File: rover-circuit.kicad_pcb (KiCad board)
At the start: 4 copper layers, 78 x 75.3 mm, 64 parts, among them J1 Battery Connector, J2 USB_C_Receptacle_USB2.0_14P, J3 Conn_01x04, J5 Raspberry_Pi_2_3, J6 Conn_02x07_Odd_Even, M1 Motor_DC, M2 Motor_DC, SW1 SW_EN, SW2 SW_IO0, U1 ESP32-C6-MINI-1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

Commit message: more on routing and schematic
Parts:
- added C10: 100uF, Capacitor_SMD:CP_Elec_6.3x5.4, F.Cu at (149.3, 74.8)
- added C11: 10uF, Capacitor_SMD:C_0805_2012Metric, F.Cu at (153.9, 79.5)
- added C8: 2.2uF, Capacitor_SMD:C_0603_1608Metric, F.Cu at (144.3, 77.8)
- added C9: 10nF, Capacitor_SMD:C_0603_1608Metric, F.Cu at (139.2, 79.0)
- added R10: 200m, Resistor_SMD:R_1206_3216Metric, F.Cu at (144.3, 74.0)
- added R9: 200m, Resistor_SMD:R_1206_3216Metric, F.Cu at (136.4, 74.0)
- added U10: LTC2954CDDB-1-PBF, Package_DFN_QFN:DFN-8-1EP_2x3mm_P0.5mm_EP0.61x2.2mm, F.Cu at (137.7, 90.9)
- moved C26 188.1 mm to (139.9, 91.7), turned to -90 degrees
- moved C21 25.1 mm to (129.4, 98.3), turned to 0 degrees
- moved C22 25.1 mm to (133.1, 91.6), turned to 180 degrees
- moved L3 23.6 mm to (128.2, 94.4), turned to 180 degrees
- moved C20 21.7 mm to (129.4, 100.3), turned to 0 degrees
- moved U7 19.4 mm to (133.7, 94.4), turned to 180 degrees
- moved C18 15.5 mm to (141.7, 97.2), turned to 90 degrees
- moved C19 15.0 mm to (132.7, 96.9)
- moved C28 12.5 mm to (144.4, 93.8), turned to 180 degrees
- moved C17 11.7 mm to (144.4, 95.8), turned to 180 degrees
- moved U9 11.5 mm to (144.5, 98.4), turned to 0 degrees
- moved D2 10.8 mm to (124.9, 68.6), turned to 150 degrees
- moved D1 10.7 mm to (124.0, 70.2), turned to 150 degrees
- moved R8 9.21 mm to (127.6, 70.1), turned to -30 degrees
- moved R1 9.14 mm to (126.7, 71.7), turned to -30 degrees
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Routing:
- net /Battery Recharger/CBSET_PIN: track 34.5 -> 0.00 mm, vias 2 -> 0
- net /Power Rails/EN: track 0.00 -> 24.2 mm, vias 0 -> 4
- net /Battery Recharger/TS: track 26.5 -> 4.53 mm, vias 1 -> 0
- net /Battery Recharger/REGN: track 19.8 -> 6.03 mm, vias 2 -> 0
- net Net-(U2-~{PG}): track 12.9 -> 0.00 mm
- net Net-(U2-STAT): track 12.1 -> 0.00 mm
- net +5V: track 0.00 -> 9.24 mm, vias 1 -> 2
- net Net-(M2--): track 0.00 -> 8.65 mm
- net Net-(M2-+): track 0.00 -> 8.51 mm
- net Net-(M1-+): track 0.00 -> 8.48 mm
- net Net-(M1--): track 0.00 -> 8.35 mm
- net Net-(U3-BISEN): track 0.00 -> 7.67 mm, vias 0 -> 4
- net Net-(U3-AISEN): track 0.00 -> 7.60 mm, vias 0 -> 5
- net Net-(U7-SW): track 0.00 -> 5.64 mm
- net Net-(U9-SW): track 0.00 -> 2.49 mm
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- removed copper zone on F.Cu, net +3V3
- removed copper zone on B.Cu, net +BATT
- removed copper zone on F.Cu, net Net-(U7-SW)
- removed copper zone on B.Cu, net VBUS

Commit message: some improvements
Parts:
- moved C11 10.6 mm to (143.5, 81.2), turned to -90 degrees
- moved J1 0.69 mm to (135.6, 62.2)
- moved U1 0.51 mm to (173.8, 63.4)
- moved C1 0.51 mm to (165.6, 61.0)
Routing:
- net /Battery Recharger/CBSET_PIN: track 0.00 -> 32.2 mm, vias 0 -> 1
- net /Battery Recharger/REGN: track 6.03 -> 22.1 mm, vias 0 -> 2
- net /Battery Recharger/TS: track 4.53 -> 20.5 mm, vias 0 -> 1
- net Net-(U2-~{PG}): track 0.00 -> 11.7 mm
- net +6V: track 1.84 -> 13.5 mm, vias 0 -> 2
- net Net-(U2-STAT): track 0.00 -> 11.2 mm
- net /Power Rails/EN: track 24.2 -> 29.1 mm, vias 4 -> 3
- net /Battery Recharger/SCL: track 0.00 -> 4.64 mm, vias 0 -> 1
- net Net-(U3-VINT): track 0.00 -> 4.37 mm
- net /Battery Recharger/SDA: track 0.00 -> 3.79 mm, vias 0 -> 1
- net /Battery Recharger/CD: track 0.00 -> 2.92 mm, vias 0 -> 1
- net Net-(U5-BST): track 0.00 -> 1.80 mm
- net VBUS: vias 0 -> 4
- net GND: vias 10 -> 11
- net +BATT: vias 0 -> 19
- added copper zone on B.Cu, net +BATT
- added copper zone on B.Cu, net VBUS

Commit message: updates
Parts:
- added SW3: SW_Push, Button_Switch_SMD:SW_SPST_B3U-1000P, F.Cu at (225.5, 122.2)
- moved SW1 172.4 mm to (163.1, 66.8), turned to 90 degrees
- moved J6 161.5 mm to (149.1, 115.4)
- moved SW2 150.8 mm to (185.3, 71.9), turned to 180 degrees
- moved D3 65.3 mm to (151.5, 93.8)
- moved R15 65.3 mm to (148.4, 93.8)
- moved J1 2.06 mm to (137.6, 62.2)
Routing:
- net /Rasbpberry PI/SDA: track 0.00 -> 25.2 mm
- net +5V: track 9.24 -> 30.6 mm
- net /Rasbpberry PI/SCL: track 0.00 -> 19.5 mm
- net /Battery Recharger/CBSET_IN: track 0.00 -> 8.79 mm
- net /Battery Recharger/CBSET_PIN: track 32.2 -> 28.2 mm
- net Net-(U5-SW): track 1.80 -> 0.00 mm
- net /Battery Recharger/REGN: track 22.1 -> 21.3 mm
- net /Battery Recharger/TS: track 20.5 -> 20.3 mm, vias 1 -> 2
- net VBUS: vias 4 -> 8
- net GND: vias 11 -> 16
- removed copper zone on F.Cu, net /Battery Recharger/CBSET_IN

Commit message: progress on routing
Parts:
- added C27: 0.1uF, Resistor_SMD:R_0805_2012Metric, F.Cu at (165.5, 66.3)
- added C29: 100nF, Capacitor_SMD:C_0603_1608Metric, F.Cu at (215.8, 85.2)
- added C30: 100nF, Capacitor_SMD:C_0603_1608Metric, F.Cu at (215.8, 87.7)
- added R16: 4.7k, Resistor_SMD:R_0603_1608Metric, F.Cu at (153.3, 63.7)
- added R17: 4.7k, Resistor_SMD:R_0603_1608Metric, F.Cu at (155.9, 63.7)
- added R18: 10k, Resistor_SMD:R_0603_1608Metric, F.Cu at (221.8, 85.2)
- added R19: 470, Resistor_SMD:R_0603_1608Metric, F.Cu at (221.8, 87.7)
- added R20: 470, Resistor_SMD:R_0603_1608Metric, F.Cu at (221.8, 90.2)
- added U11: BMI270, Package_LGA:Bosch_LGA-14_3x2.5mm_P0.5mm, F.Cu at (237.2, 74.5)
- U1: value ESP32-C6-MINI-1 -> MMC5983MA; footprint RF_Module:ESP32-C6-MINI-1 -> Package_LGA:LGA-16_3x3mm_P0.5mm
- U6: value MPU-6050 -> ESP32-C6-WROOM-1-N8; footprint Sensor_Motion:InvenSense_QFN-24_4x4mm_P0.5mm -> lib_fp:XCVR_ESP32-C6-WROOM-1-N8
- moved U6 194.5 mm to (182.2, 86.0), turned to -90 degrees
- moved SW3 106.2 mm to (124.7, 88.7), turned to 0 degrees
- moved U1 66.9 mm to (236.9, 85.5)
- moved SW1 45.8 mm to (208.7, 71.5)
- moved DWM1 28.0 mm to (174.4, 59.6), turned to 0 degrees
- moved SW2 19.9 mm to (205.2, 71.5), turned to 90 degrees
- moved J6 4.01 mm to (145.3, 114.2)
- moved C1 3.13 mm to (163.3, 59.0), turned to 90 degrees
- moved R3 0.58 mm to (129.1, 76.4)
- moved C6 0.51 mm to (125.4, 84.4)
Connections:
- net /Battery Recharger/~{INT} renamed Net-(U2-~{INT})
- net /Motor Driver/AIN1 renamed /MCU/AIN1
- net /Motor Driver/AIN2 renamed /MCU/AIN2
- net /Motor Driver/BIN1 renamed /MCU/BIN1
- net /Motor Driver/BIN2 renamed /MCU/BIN2
- net /UWB/UWB_RST renamed /MCU/UWB_RST
- net /UWB/UWB_WAKEUP renamed /MCU/UWB_WUP
- net /UWB/UWB_~{CS} renamed /MCU/UWB_~{CS}
- DWM1 pad 22: /UWB/UWB_IRQ -> /MCU/UWB_IRQ
- R3 pad 1: +3V3 -> /Battery Recharger/REGN
- SW2 pad 2: /MCU/IO0 -> /MCU/IO9
- U1 pad 1: GND -> /Battery Recharger/SCL
- U1 pad 10: unconnected-(U1-IO5-Pad10) -> Net-(U1-CAP)
- U1 pad 13: unconnected-(U1-IO1-Pad13) -> +3V3
- U1 pad 14: GND -> unconnected-(U1-NC-Pad14)
- U1 pad 15: /Battery Recharger/SDA -> unconnected-(U1-INT-Pad15)
- U1 pad 16: /Battery Recharger/SCL -> /Battery Recharger/SDA
- U1 pad 2: GND -> +3V3
- U1 pad 3: +3V3 -> unconnected-(U1-NC-Pad3)
- U1 pad 4: unconnected-(U1-NC-Pad4) -> +3V3
- U1 pad 8: /MCU/EN -> unconnected-(U1-NC-Pad8)
- U1 pad 9: unconnected-(U1-IO4-Pad9) -> GND
- U2 pad 24: /Battery Recharger/PSEL -> unconnected-(U2-PSEL-Pad24)
- U2 pad 3: /Battery Recharger/CD -> unconnected-(U2-CD-Pad3)
- U6 pad 10: Net-(U6-REGOUT) -> unconnected-(U6-IO8-Pad10)
- U6 pad 11: GND -> unconnected-(U6-IO10-Pad11)
- U6 pad 13: +3V3 -> /MCU/USB1.D-
- U6 pad 14: unconnected-(U6-NC-Pad14) -> /MCU/USB1.D+
- U6 pad 15: unconnected-(U6-NC-Pad15) -> /MCU/IO9
- U6 pad 18: GND -> unconnected-(U6-IO20-Pad18)
- U6 pad 2: unconnected-(U6-NC-Pad2) -> +3V3
- U6 pad 20: Net-(U6-CPOUT) -> unconnected-(U6-IO22-Pad20)
- U6 pad 23: /Battery Recharger/SCL -> unconnected-(U6-IO15-Pad23)
- U6 pad 24: /Battery Recharger/SDA -> /MCU/RX0
- U6 pad 3: unconnected-(U6-NC-Pad3) -> /MCU/EN
- U6 pad 8: Net-(U6-VLOGIC) -> unconnected-(U6-IO0-Pad8)
- U6 pad 9: GND -> unconnected-(U6-IO1-Pad9)
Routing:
- net /Battery Recharger/SCL: track 4.64 -> 47.3 mm, vias 1 -> 2
- net /Battery Recharger/SDA: track 3.79 -> 42.7 mm, vias 1 -> 2
- net /Rasbpberry PI/SDA: track 25.2 -> 0.00 mm
- net /Rasbpberry PI/SCL: track 19.5 -> 0.00 mm
- net +5V: track 30.6 -> 19.7 mm
- net Net-(D3-K): track 0.00 -> 10.4 mm, vias 0 -> 2
- net /MCU/USB1.D+: track 0.00 -> 8.80 mm, vias 0 -> 1
- net /MCU/USB1.D-: track 0.00 -> 8.53 mm, vias 0 -> 1
- net /MCU/BIN1: track 0.00 -> 7.32 mm, vias 0 -> 1
- net /MCU/BIN2: track 0.00 -> 6.45 mm, vias 0 -> 1
- net /Battery Recharger/REGN: track 21.3 -> 27.6 mm, vias 2 -> 3
- net +3V3: track 0.50 -> 6.34 mm, vias 0 -> 2
- net /Battery Recharger/CD: track 2.92 -> 0.00 mm, vias 1 -> 0
- net /MCU/AIN2: track 0.00 -> 2.74 mm, vias 0 -> 1
- net /MCU/AIN1: track 0.00 -> 2.07 mm, vias 0 -> 1
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- added copper zone on F.Cu, net +3V3

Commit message: progress on routing
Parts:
- added C14: 10uF, Capacitor_SMD:C_0603_1608Metric, F.Cu at (167.2, 90.8)
- added C15: 10uF, Capacitor_SMD:C_0603_1608Metric, F.Cu at (167.1, 86.9)
- added D5: BLUE, LED_SMD:LED_0603_1608Metric, F.Cu at (164.7, 75.0)
- added D6: BLUE, LED_SMD:LED_0603_1608Metric, F.Cu at (164.7, 73.3)
- C1: footprint Capacitor_SMD:C_0402_1005Metric -> Capacitor_SMD:C_0805_2012Metric
- moved U11 78.3 mm to (159.5, 83.8)
- moved U1 72.4 mm to (164.6, 89.7)
- moved C30 59.3 mm to (156.6, 83.8), turned to -90 degrees
- moved SW1 56.8 mm to (157.3, 95.8)
- moved C29 55.1 mm to (160.8, 81.3)
- moved R20 50.8 mm to (173.7, 74.1), turned to -90 degrees
- moved SW2 49.6 mm to (162.0, 95.8)
- moved R19 48.6 mm to (175.2, 74.1), turned to -90 degrees
- moved R18 44.3 mm to (184.3, 61.6)
- moved SW3 37.4 mm to (157.2, 70.1), turned to 180 degrees
- moved C1 28.5 mm to (187.2, 74.6), turned to 0 degrees
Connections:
- U6 pad 10: unconnected-(U6-IO8-Pad10) -> /MCU/AIN2
- U6 pad 11: unconnected-(U6-IO10-Pad11) -> /MCU/AIN1
- U6 pad 12: unconnected-(U6-IO11-Pad12) -> /Motor Driver/SLEEP
- U6 pad 23: unconnected-(U6-IO15-Pad23) -> /MCU/UWB_RST
- U6 pad 26: unconnected-(U6-IO3-Pad26) -> /MCU/UWB_WUP
- U6 pad 27: unconnected-(U6-IO2-Pad27) -> /MCU/UWB_IRQ
- U6 pad 4: unconnected-(U6-IO4-Pad4) -> /MCU/CLK
- U6 pad 5: unconnected-(U6-IO5-Pad5) -> /MCU/MISO
- U6 pad 6: unconnected-(U6-IO6-Pad6) -> /MCU/MOSI
- U6 pad 7: unconnected-(U6-IO7-Pad7) -> /MCU/UWB_~{CS}
- U6 pad 8: unconnected-(U6-IO0-Pad8) -> /MCU/BIN1
- U6 pad 9: unconnected-(U6-IO1-Pad9) -> /MCU/BIN2
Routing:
- net +3V3: track 6.34 -> 140.1 mm
- net /MCU/USB1.D-: track 8.53 -> 65.8 mm, vias 1 -> 2
- net /MCU/USB1.D+: track 8.80 -> 65.0 mm, vias 1 -> 2
- net /MCU/RX0: track 0.00 -> 53.7 mm
- net /MCU/TX0: track 0.00 -> 51.4 mm
- net /MCU/UWB_WUP: track 0.00 -> 48.0 mm, vias 0 -> 2
- net /MCU/UWB_RST: track 0.00 -> 47.0 mm, vias 0 -> 2
- net /Battery Recharger/SCL: track 47.3 -> 86.9 mm
- net /Battery Recharger/SDA: track 42.7 -> 80.9 mm
- net /Motor Driver/SLEEP: track 2.07 -> 40.2 mm, vias 1 -> 2
- net /MCU/BIN1: track 7.32 -> 44.9 mm, vias 1 -> 2
- net /MCU/UWB_IRQ: track 0.00 -> 37.4 mm, vias 0 -> 2
- net /MCU/BIN2: track 6.45 -> 42.6 mm, vias 1 -> 2
- net /MCU/AIN2: track 2.74 -> 37.7 mm, vias 1 -> 2
- net /MCU/AIN1: track 2.07 -> 35.7 mm, vias 1 -> 2
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
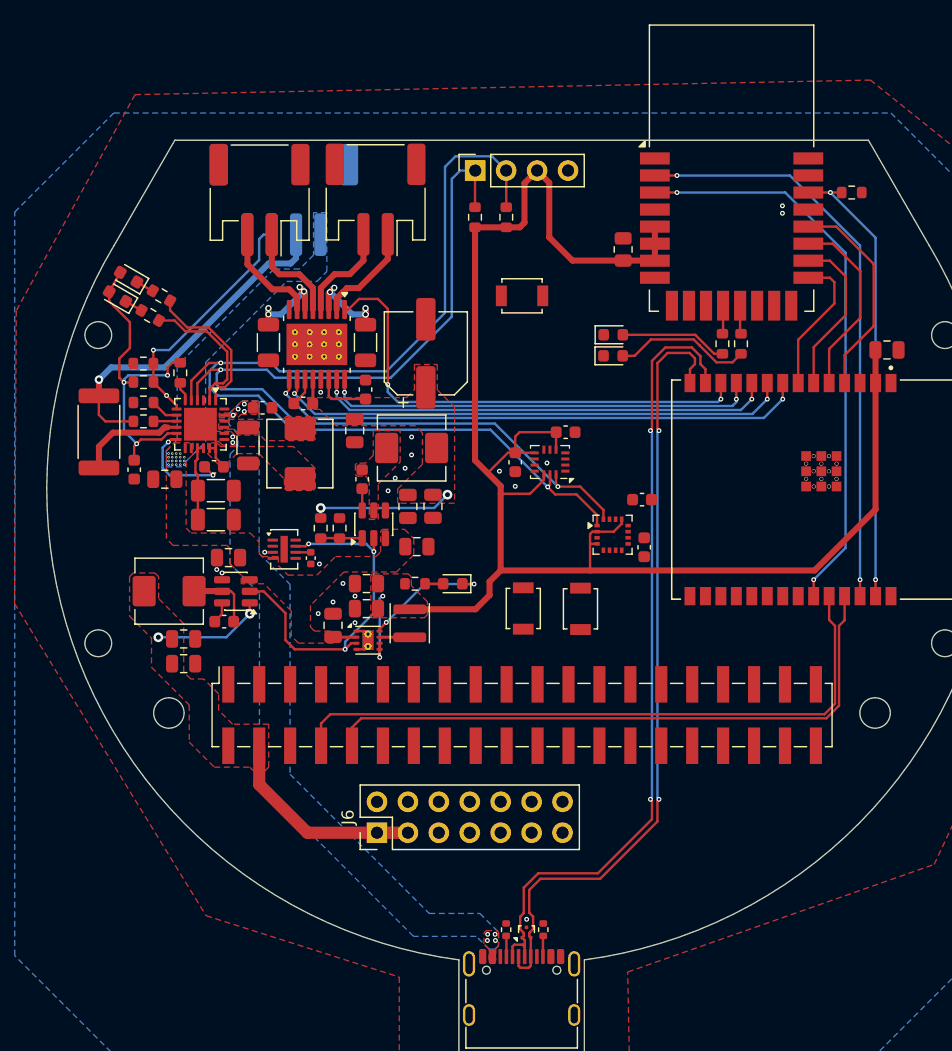
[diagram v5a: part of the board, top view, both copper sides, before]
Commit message: consolidated routing
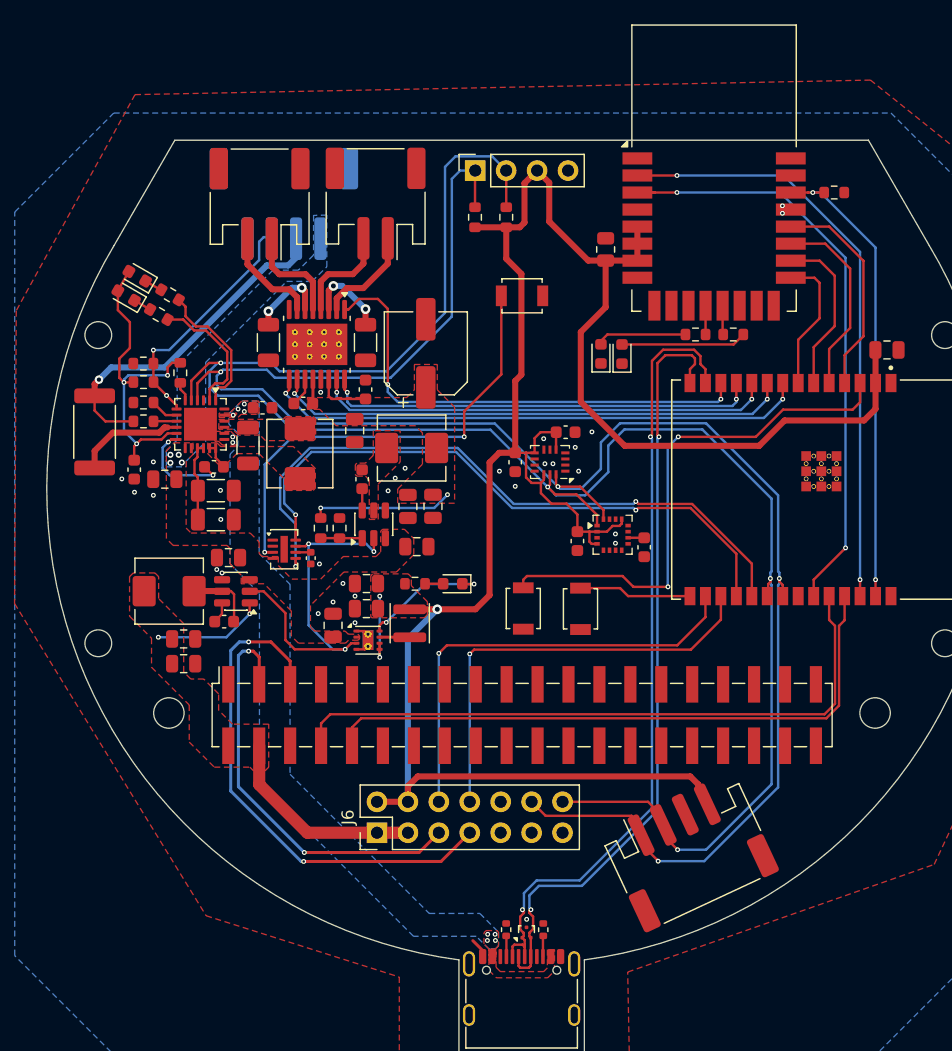
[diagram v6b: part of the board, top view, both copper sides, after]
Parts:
- added J4: Conn_01x04_Socket, Connector_JST:JST_PH_S4B-PH-SM4-TB_1x04-1MP_P2.00mm_Horizontal, F.Cu at (170.9, 115.7)
- moved C15 6.31 mm to (161.7, 90.3), turned to -90 degrees
- moved R20 2.34 mm to (171.5, 73.3), turned to 180 degrees
- moved D6 1.87 mm to (163.7, 74.9), turned to 90 degrees
- moved C27 1.44 mm to (164.1, 66.3)
- moved DWM1 1.44 mm to (173.0, 59.6)
- moved R18 1.44 mm to (182.8, 61.6)
- moved R19 0.99 mm to (174.5, 73.3), turned to 0 degrees
- moved D5 0.74 mm to (165.4, 74.9), turned to 90 degrees
- moved D1 0.71 mm to (124.7, 70.1)
- moved D2 0.71 mm to (125.6, 68.5)
- moved R1 0.71 mm to (127.4, 71.7)
- moved R8 0.71 mm to (128.3, 70.0)
- moved R5 0.36 mm to (122.1, 81.3)
- moved J1 0.33 mm to (137.6, 62.6)
- moved M1 0.33 mm to (145.2, 62.5)
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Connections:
- J5 pad 11: /Rasbpberry PI/DC -> unconnected-(J5-GPIO17-Pad11)
- J5 pad 12: /Rasbpberry PI/PWMA_1 -> unconnected-(J5-GPIO18/PWM0-Pad12)
- J5 pad 13: /Rasbpberry PI/RES -> unconnected-(J5-GPIO27-Pad13)
- J5 pad 15: /Rasbpberry PI/UWB_~{RST} -> unconnected-(J5-GPIO22-Pad15)
- J5 pad 16: /Rasbpberry PI/AIN2_1 -> unconnected-(J5-GPIO23-Pad16)
- J5 pad 18: /Rasbpberry PI/UWB_WU -> unconnected-(J5-GPIO24-Pad18)
- J5 pad 19: /Rasbpberry PI/MOSI -> unconnected-(J5-MOSI0/GPIO10-Pad19)
- J5 pad 21: /Rasbpberry PI/MISO -> unconnected-(J5-MISO0/GPIO9-Pad21)
- J5 pad 22: /Rasbpberry PI/AIN1_1 -> unconnected-(J5-GPIO25-Pad22)
- J5 pad 23: /Rasbpberry PI/CLK -> unconnected-(J5-SCLK0/GPIO11-Pad23)
- J5 pad 24: /Rasbpberry PI/UWB_~{CS} -> unconnected-(J5-~{CE0}/GPIO8-Pad24)
- J5 pad 26: /Rasbpberry PI/UWB_IRQ -> unconnected-(J5-~{CE1}/GPIO7-Pad26)
- J5 pad 27: /Rasbpberry PI/STBYB -> unconnected-(J5-ID_SD/GPIO0-Pad27)
- J5 pad 28: /Rasbpberry PI/BIN1_1 -> unconnected-(J5-ID_SC/GPIO1-Pad28)
- J5 pad 29: /Rasbpberry PI/BIN2_1 -> unconnected-(J5-GCLK1/GPIO5-Pad29)
- J5 pad 3: /Rasbpberry PI/SDA -> Net-(J5-SDA/GPIO2)
- J5 pad 31: /Rasbpberry PI/AIN2_2 -> unconnected-(J5-GCLK2/GPIO6-Pad31)
- J5 pad 32: /Rasbpberry PI/PWMB_1 -> unconnected-(J5-PWM0/GPIO12-Pad32)
- J5 pad 33: /Rasbpberry PI/PWMA_2 -> unconnected-(J5-PWM1/GPIO13-Pad33)
- J5 pad 35: /Rasbpberry PI/PWMB_2 -> unconnected-(J5-GPIO19/MISO1-Pad35)
- J5 pad 36: /Rasbpberry PI/AIN1_2 -> unconnected-(J5-GPIO16-Pad36)
- J5 pad 37: /Rasbpberry PI/BIN2_2 -> unconnected-(J5-GPIO26-Pad37)
- J5 pad 38: /Rasbpberry PI/STBYA -> unconnected-(J5-GPIO20/MOSI1-Pad38)
- J5 pad 40: /Rasbpberry PI/BIN1_2 -> unconnected-(J5-GPIO21/SCLK1-Pad40)
- J5 pad 5: /Rasbpberry PI/SCL -> Net-(J5-SCL/GPIO3)
- J5 pad 7: /Rasbpberry PI/CS -> unconnected-(J5-GCLK0/GPIO4-Pad7)
- J6 pad 10: /Rasbpberry PI/CLK -> unconnected-(J6-Pin_10-Pad10)
- J6 pad 12: /Rasbpberry PI/MISO -> /Battery Recharger/SDA
- J6 pad 14: /Rasbpberry PI/MOSI -> /Battery Recharger/SCL
- J6 pad 2: /Rasbpberry PI/SCL -> +3V3
- J6 pad 4: /Rasbpberry PI/SDA -> +3V3
- J6 pad 5: +3V3 -> Net-(J5-SDA/GPIO2)
- J6 pad 6: /Rasbpberry PI/GPIO_18 -> /MCU/IO18
- J6 pad 7: +3V3 -> Net-(J5-SCL/GPIO3)
- J6 pad 8: /Rasbpberry PI/GPIO_8 -> /MCU/IO19
- U10 pad 5: /Power Rails/~{KILL} -> /MCU/~{KILL}
- U10 pad 8: /Power Rails/~{INT} -> /MCU/~{INT}
- U6 pad 16: unconnected-(U6-IO18-Pad16) -> /MCU/IO18
- U6 pad 17: unconnected-(U6-IO19-Pad17) -> /MCU/IO19
- U6 pad 18: unconnected-(U6-IO20-Pad18) -> /MCU/~{INT}
- U6 pad 19: unconnected-(U6-IO21-Pad19) -> /MCU/~{KILL}
- U6 pad 20: unconnected-(U6-IO22-Pad20) -> /Battery Recharger/SCL
- U6 pad 21: unconnected-(U6-IO23-Pad21) -> /Battery Recharger/SDA
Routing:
- net /Battery Recharger/SDA: track 80.9 -> 156.1 mm, vias 2 -> 4
- net /Battery Recharger/SCL: track 86.9 -> 158.4 mm, vias 2 -> 4
- net /MCU/~{KILL}: track 0.00 -> 55.0 mm, vias 0 -> 2
- net /MCU/~{INT}: track 0.00 -> 50.5 mm, vias 0 -> 2
- net +3V3: track 140.1 -> 184.2 mm, vias 2 -> 3
- net /MCU/EN: track 0.00 -> 43.4 mm, vias 0 -> 2
- net Net-(J5-SCL/GPIO3): track 0.00 -> 42.3 mm, vias 0 -> 2
- net Net-(U10-~{PB}): track 0.66 -> 38.0 mm, vias 1 -> 2
- net /MCU/IO18: track 0.00 -> 37.0 mm, vias 0 -> 1
- net /MCU/IO19: track 0.00 -> 35.9 mm, vias 0 -> 1
- net Net-(J5-SDA/GPIO2): track 0.00 -> 34.4 mm, vias 0 -> 2
- net /MCU/IO9: track 0.00 -> 9.26 mm
- net /MCU/UWB_RST: track 47.0 -> 49.6 mm
- net +BATT: track 1.93 -> 0.03 mm, vias 19 -> 4
- net Net-(D6-A): track 8.83 -> 7.16 mm
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
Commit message: complete routing and validated ERC/DRC
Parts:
- C27: footprint Resistor_SMD:R_0805_2012Metric -> Capacitor_SMD:C_0805_2012Metric
- moved J4 2.01 mm to (169.1, 114.8), turned to 0 degrees
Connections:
- net /Motor Driver/SLEEP renamed /MCU/~{SLEEP}
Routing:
- net +3V3: track 184.2 -> 174.2 mm
- net /Battery Recharger/SCL: track 158.4 -> 161.9 mm
- net /Battery Recharger/SDA: track 156.1 -> 157.9 mm
- net GND: track 3.75 -> 2.11 mm
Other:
- copper layers 4 -> 2
